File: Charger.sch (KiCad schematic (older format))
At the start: 65 parts, among them Q1 AO4407A, Q10 AON7400A, Q11 AON7400A, Q8 AON7400A, Q9 AON7400A, U1 bq2477x

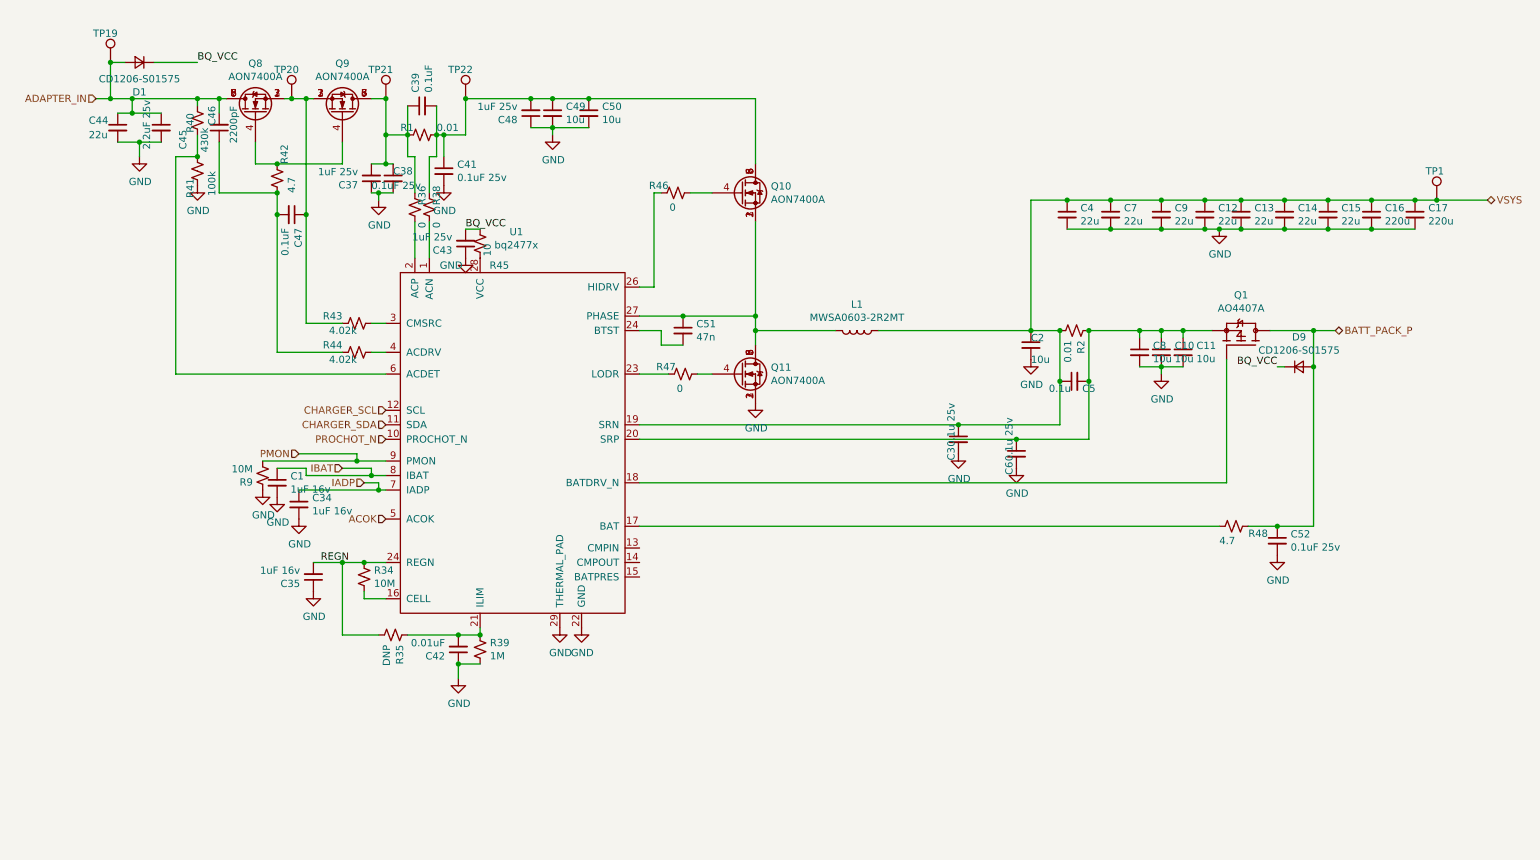
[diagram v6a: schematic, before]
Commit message: Replaced old charger to support JLC assembly. Very close now!
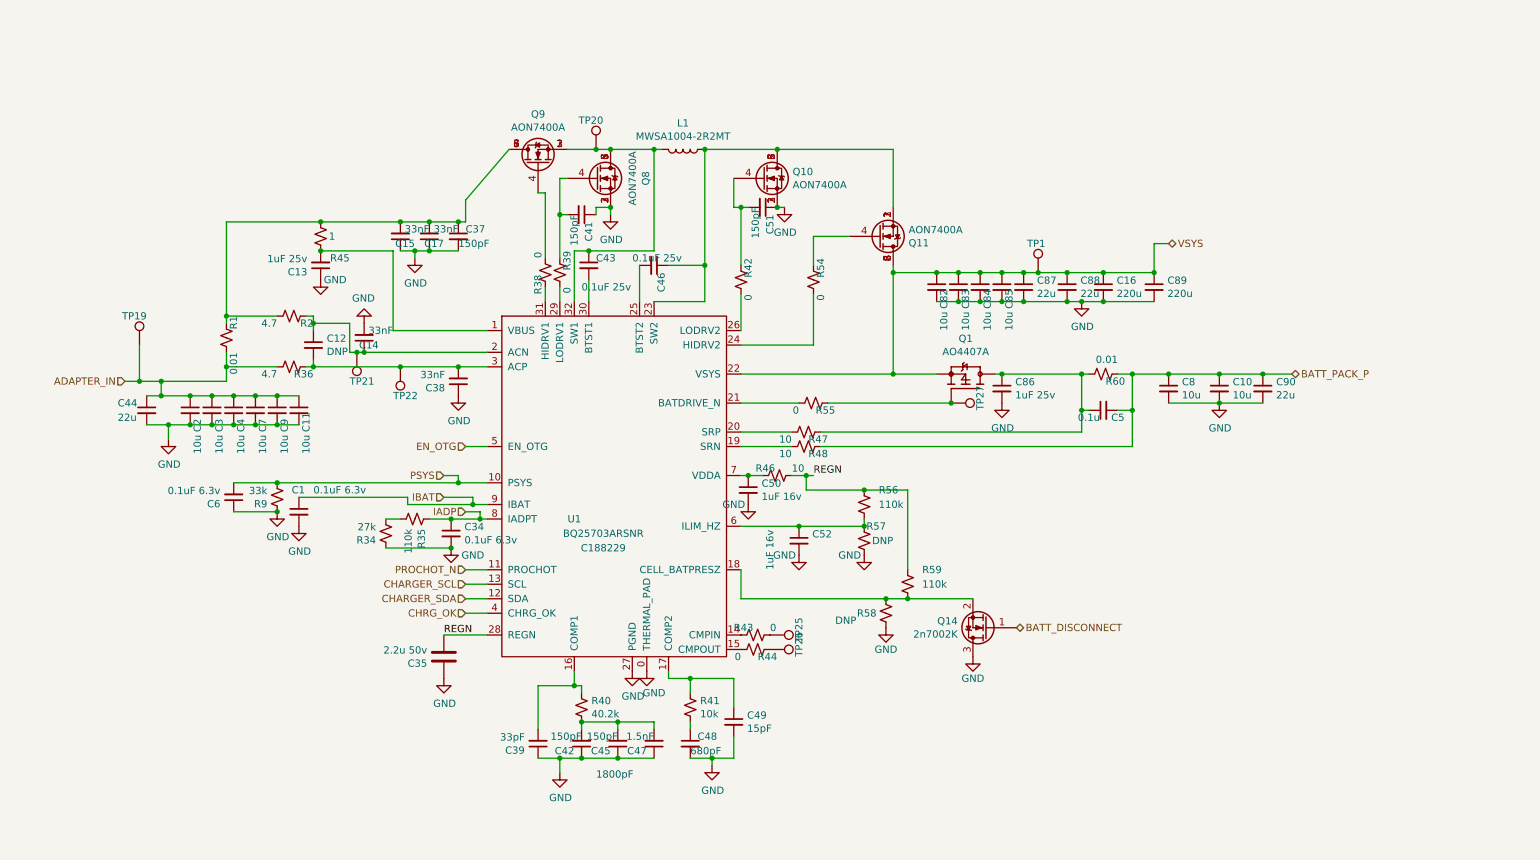
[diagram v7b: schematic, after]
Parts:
- removed C35: 1uF 16v, lc_lib:0402_C, symbol Device:C_Small
- removed D1, D9: CD1206-S01575, lc_lib:SOD-123, symbol Device:D_Small
- removed U1: bq2477x, SmartBattery:QFN40P400X400X80-29N, symbol SmartBattery:bq2477x
- added C35: 2.2u 50v, lc_lib:0805_C, symbol Device:C
- added C82, C83, C84, C85: 10u, lc_lib:0805_C, symbol Device:C_Small
- added C86: 1uF 25v, lc_lib:0402_C, symbol Device:C_Small
- added C87, C88, C90: 22u, lc_lib:0805_C, symbol Device:C_Small
- added C89: 220u, Capacitor_SMD:C_Elec_8x10.2, symbol Device:C_Small
- added Q14: 2n7002K, Package_TO_SOT_SMD:SOT-23, symbol Device:Q_NMOS_GSD
- added R54, R55: 0, lc_lib:0402_R, symbol Device:R_Small_US
- added R56, R59: 110k, lc_lib:0402_R, symbol Device:R_Small_US
- added R57, R58: DNP, lc_lib:0402_R, symbol Device:R_Small_US
- added R60: 0.01, lc_lib:2512_R, symbol Device:R_Small_US
- added TP25, TP26, TP27: TestPoint, TestPoint:TestPoint_Pad_D2.0mm, symbol Connector:TestPoint
- added U1: BQ25703ARSNR, lc_lib:VQFN-32_4X4X04P, symbol SmartBattery:BQ25703ARSNR
- C1: value 1uF 16v -> 0.1uF 6.3v; LCSC C52923 -> C1525
- C11: LCSC (none) -> C15850; SKU CC0805KKX5R8BB106 -> (none)
- C12: value 22u -> DNP; footprint lc_lib:0805_C -> lc_lib:0402_C; SKU CL21A226MAQNNNE -> (none)
- C13: value 22u -> 1uF 25v; footprint lc_lib:0805_C -> lc_lib:0402_C; SKU CL21A226MAQNNNE -> (none); lcsc (none) -> C52923
- C14, C15: value 22u -> 33nF; footprint lc_lib:0805_C -> lc_lib:0402_C; LCSC (none) -> C1585; SKU CL21A226MAQNNNE -> (none)
- C16: LCSC (none) -> C311611; SKU RVT1V221M0810 -> (none)
- C17: value 220u -> 33nF; footprint Capacitor_SMD:C_Elec_8x10.2 -> lc_lib:0402_C; LCSC (none) -> C1585; SKU RVT1V221M0810 -> (none)
- C3: value 0.1u 25v -> 10u; footprint lc_lib:0402_C -> lc_lib:0805_C; LCSC (none) -> C15850
- C34: value 1uF 16v -> 0.1uF 6.3v; lcsc (none) -> C1525
- C37: value 1uF 25v -> 150pF; lcsc (none) -> C1527
- C38: value 0.1uF 25v -> 33nF; LCSC (none) -> C1585
- C39: value 0.1uF -> 33pF; LCSC (none) -> C1562
- C4, C7, C9: value 22u -> 10u; LCSC (none) -> C15850; SKU CL21A226MAQNNNE -> (none)
- C41: value 0.1uF 25v -> 150pF; lcsc (none) -> C1527
- C42: value 0.01uF -> 150pF; lcsc (none) -> C1527
- C43: value 1uF 25v -> 0.1uF 25v; lcsc (none) -> C1525
- C44: LCSC (none) -> C45783; SKU CL21A226MAQNNNE -> (none)
- C45: value 2.2uF 25v -> 150pF; footprint lc_lib:0805_C -> lc_lib:0402_C; lcsc (none) -> C1527
- C46: value 2200pF -> 0.1uF 25v; lcsc (none) -> C1525
- C47: value 0.1uF -> 1.5nF; lcsc (none) -> C23967
- C48: value 1uF 25v -> 680pF; footprint lc_lib:0402_C -> lc_lib:0603_C; SKU CC0805KKX5R8BB106 -> (none); lcsc (none) -> C1630
- C49: value 10u -> 15pF; footprint lc_lib:0805_C -> lc_lib:0402_C; LCSC (none) -> C1548; SKU CC0805KKX5R8BB106 -> (none)
- C50: value 10u -> 1uF 16v; footprint lc_lib:0805_C -> lc_lib:0402_C; SKU CC0805KKX5R8BB106 -> (none); lcsc (none) -> C52923
- C51: value 47n -> 150pF; lcsc (none) -> C1527
- C52: value 0.1uF 25v -> 1uF 16v; lcsc (none) -> C52923
- C6: value 0.1u 25v -> 0.1uF 6.3v; lcsc (none) -> C1525
- L1: value MWSA0603-2R2MT -> MWSA1004-2R2MT; footprint SmartBattery:MWSA0603 -> SmartBattery:L_10.3x11.5_H4; LCSC (none) -> C149550; SKU MWSA0603-2R2MT -> (none)
- Q1: LCSC (none) -> C16072
- Q10, Q11, Q8, Q9: LCSC (none) -> C85734; SKU AON7400A -> (none)
- R1: lcsc (none) -> C127692
- R2: value 0.01 -> 4.7; footprint lc_lib:2512_R -> lc_lib:0402_R; lcsc (none) -> C23164
- R34: value 10M -> 27k; footprint lc_lib:0402_R -> lc_lib:0603_R; lcsc (none) -> C25771
- R35: value DNP -> 110k; footprint lc_lib:0402_R -> lc_lib:0603_R; lcsc (none) -> C25805
- R36: value 0 -> 4.7; lcsc (none) -> C23164
- R39: value 1M -> 0
- R40: value 430k -> 40.2k; footprint lc_lib:0402_R -> lc_lib:0603_R; lcsc (none) -> C12447
- R41: value 100k -> 10k; lcsc (none) -> C25744
- R42: value 4.7 -> 0
- R43, R44: value 4.02k -> 0
- R45: value 10 -> 1; lcsc (none) -> C25086
- R46, R47: value 0 -> 10; lcsc (none) -> C25123
- R48: value 4.7 -> 10; lcsc (none) -> C25123
- R9: value 10M -> 33k; lcsc (none) -> C25779
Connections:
- net ADAPTER_IN: now also C11.1, C2.1, C3.1, C4.1, C7.1, C9.1, R1.1, R36.1; no longer C45.1, C46.2, Q8.5 (D), Q8.6 (D), Q8.7 (D), Q8.8 (D), R40.2
- net BATT_PACK_P: now also C10.1, C5.2, C8.1, R48.2, C90.1, R60.2; no longer C52.1, Q1.5, Q1.6, Q1.7, Q1.8, R48.1
- net CHARGER_SCL: now also U1.13 (SCL)
- net CHARGER_SDA: now also U1.12 (SDA)
- net GND: now also C13.1, C15.1, C17.1, C37.2, C38.1, C39.1, C41.1, C45.1, C47.1, C48.2, C51.1, C6.1, Q10.1 (S), Q10.2 (S), Q10.3 (S), Q8.1 (S), Q8.2 (S), Q8.3 (S), R34.1, C35.1, C82.2, C83.2, C84.2, C85.2, C86.2, C87.2, C88.2, C89.2, C90.2, Q14.3 (D), R57.1, R58.2, U1.0 (THERMAL_PAD), U1.27 (PGND); no longer C12.2, C13.2, C15.2, C17.2, C37.1, C38.2, C41.2, C43.1, C45.2, C48.1, C6.2, Q11.1 (S), Q11.2 (S), Q11.3 (S), R39.2, R41.1
- net IADP: now also R35.1, U1.8 (IADPT)
- net IBAT: now also U1.9 (IBAT)
- net PROCHOT_N: now also U1.11 (PROCHOT)
- net REGN: now also R46.1, C35.2, R56.1, R59.1, U1.28 (REGN); no longer R34.1, R35.2
- net VSYS: now also Q1.1, Q1.2, Q1.3, Q11.5 (D), Q11.6 (D), Q11.7 (D), Q11.8 (D), C82.1, C83.1, C84.1, C85.1, C87.1, C88.1, C89.1, U1.22 (VSYS); no longer C12.1, C13.1, C14.1, C15.1, C17.1, C2.1, C3.1, C4.1, C5.1, C7.1, C9.1, L1.1, R2.2
- net at R38.1: now also Q9.4 (G)
- net at R34.2: now also R35.2
- net at Q1.4: now also R55.2, TP27.1
- net at R47.1: now also U1.20 (SRP)
- net at C51.2: now also Q10.4 (G), R42.2
- net at R45.1: now also C13.2, U1.1 (VBUS)
- net at R43.2: now also U1.14 (CMPIN)
- net at R44.2: now also TP26.1
- net at R40.1: now also C39.2, U1.16 (COMP1); no longer R41.2
- net at Q9.5 (D), Q9.6 (D), Q9.7 (D)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: now also C15.2, C17.2, C37.1, R2.1, R45.2; no longer C37.2, C38.1, C39.1, R36.2, TP21.1
- net at R46.2: now also C50.1, U1.7 (VDDA); no longer Q10.4 (G)
- net at R47.2: now also C5.1, Q1.5, Q1.6, Q1.7, Q1.8, C86.1, R60.1; no longer Q11.4 (G)
- net BQ_VCC: no longer names the net of C43.2
- net BQ_VCC: now also U1.30 (BTST1); no longer R45.2
- net PMON renamed PSYS
- net PSYS: now also C6.2, U1.10 (PSYS)
- new net: C46.1, L1.1, Q10.5 (D), Q10.6 (D), Q10.7 (D), Q10.8 (D), Q11.1 (S), Q11.2 (S), Q11.3 (S), U1.23 (SW2)
- new net: C43.1, L1.2, Q8.5 (D), Q8.6 (D), Q8.7 (D), Q8.8 (D), Q9.1 (S), Q9.2 (S), Q9.3 (S), TP20.1, U1.32 (SW1)
- new net: C12.2, C38.2, R36.2, TP22.1, U1.3 (ACP)
- new net: C12.1, C14.1, R2.2, TP21.1, U1.2 (ACN)
- new net: R44.1, U1.15 (CMPOUT)
- new net: C49.1, R41.1, U1.17 (COMP2)
- new net: Q14.2 (S), R58.1, R59.2, U1.18 (CELL_BATPRESZ)
- new net: R48.1, U1.19 (SRN)
- new net: R55.1, U1.21 (BATDRIVE_N)
- new net: R54.1, U1.24 (HIDRV2)
- new net: C46.2, U1.25 (BTST2)
- new net: R42.1, U1.26 (LODRV2)
- new net: R39.1, U1.29 (LODRV1)
- new net: R38.2, U1.31 (HIDRV1)
- new net: C52.1, R56.2, R57.2, U1.6 (ILIM_HZ)
- new net: C42.2, C45.2, C47.2, R40.2
- new net: C48.1, R41.2
- new net: C41.2, Q8.4 (G), R39.2
- new net: Q11.4 (G), R54.2
- new net: R43.1, TP25.1
- new net BATT_DISCONNECT: Q14.1 (G)
- new net CHRG_OK: U1.4 (CHRG_OK)
- new net EN_OTG: U1.5 (EN_OTG)
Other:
- note added: "1800pF\n"
- moved on the sheet: C1, C10, C16, C34, C44, C5, C8, L1, Q1, Q10, Q11, Q8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

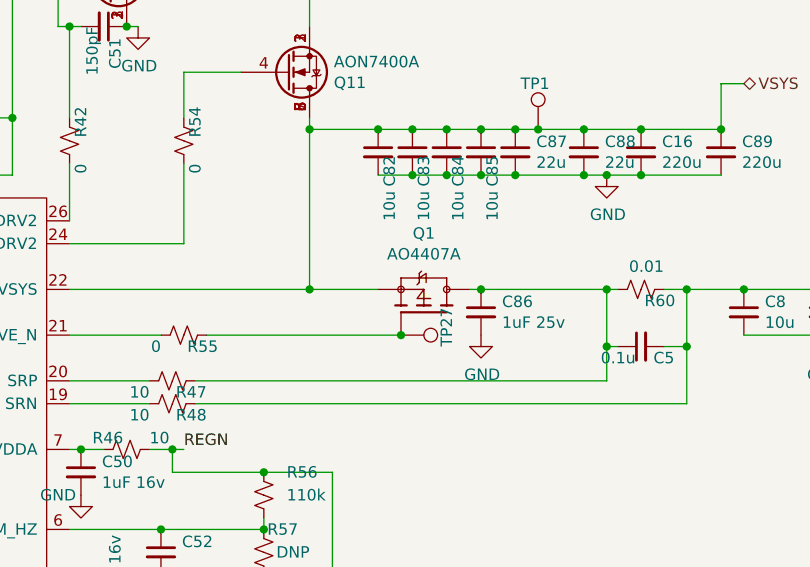
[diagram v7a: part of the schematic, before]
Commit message: Both type-c ports are done! Only outputstage left.
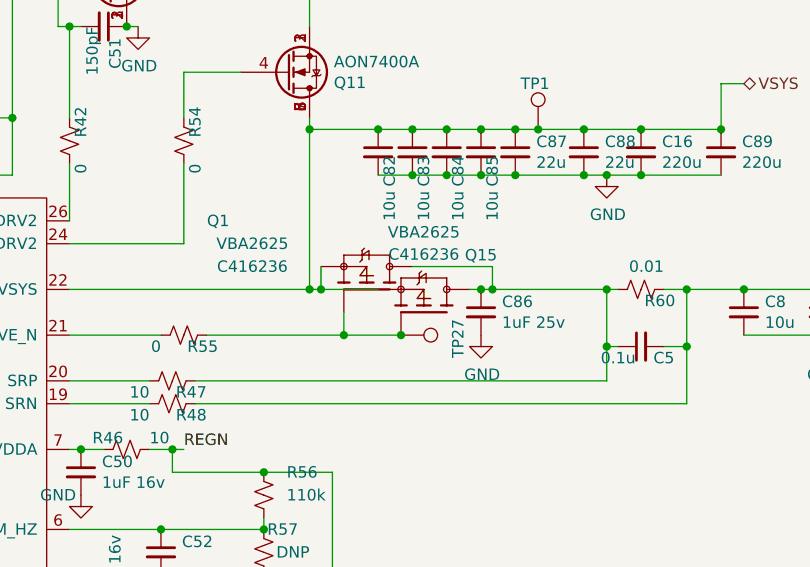
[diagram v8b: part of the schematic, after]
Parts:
- removed Q1: AO4407A, SmartBattery:SOIC127P600X175-8N, symbol SmartBattery:AO4407A
- added Q1, Q15: VBA2625, SmartBattery:SOIC127P600X175-8N, symbol SmartBattery:VBA2625
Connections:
- net VSYS: now also Q1.1, Q1.2, Q1.3, Q15.1, Q15.2, Q15.3
- net at R55.2, TP27.1: now also Q1.4, Q15.4
- net at C5.1, C86.1, R47.2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: now also Q1.5, Q1.6, Q1.7, Q1.8, Q15.5, Q15.6, Q15.7, Q15.8
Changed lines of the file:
@@
 $Descr A4 11693 8268
 encoding utf-8
-Sheet 2 6
+Sheet 2 8
 Title ""
 Date ""
@@
 Text HLabel 9250 3400 2    50   BiDi ~ 0
 BATT_PACK_P
-$Comp
-L SmartBattery:AO4407A Q1
-U 1 1 5FDAE275
-P 7000 3500
-F 0 "Q1" V 7345 3500 50  0000 C CNN
-F 1 "AO4407A" V 7254 3500 50  0000 C CNN
-F 2 "SmartBattery:SOIC127P600X175-8N" H 7000 3500 50  0001 L BNN
-F 3 "" H 7000 3500 50  0001 L BNN
-F 4 "Alpha & Omega Semiconductor" H 7000 3500 50  0001 L BNN "MANUFACTURER"
-F 5 "I" H 7000 3500 50  0001 L BNN "PARTREV"
-F 6 "IPC 7351B" H 7000 3500 50  0001 L BNN "STANDARD"
-F 7 "1.75 mm" H 7000 3500 50  0001 L BNN "MAXIMUM_PACKAGE_HEIGHT"
-F 8 "C16072" V 7000 3500 50  0001 C CNN "LCSC"
-	1    7000 3500
-	0    -1   -1   0
-$EndComp
 $Comp
 L Device:C_Small C10
@@
 Connection ~ 8300 2700
 Wire Wire Line
-	6800 3400 6500 3400
+	6800 3400 6550 3400
 Connection ~ 6500 3400
 Wire Wire Line
@@
 $EndComp
 Wire Wire Line
-	6050 3600 6900 3600
+	6050 3600 6650 3600
 $Comp
 L Connector:TestPoint TP?
@@
 AR Path="/5FD15753/60964FD3" Ref="TP?"  Part="1"
 AR Path="/5FD99B08/60964FD3" Ref="TP27"  Part="1"
-F 0 "TP27" H 6950 3800 50  0000 R CNN
+F 0 "TP27" H 7000 3850 50  0000 R CNN
 F 1 "TestPoint" H 6350 3650 50  0001 R CNN
 F 2 "TestPoint:TestPoint_Pad_D2.0mm" H 7100 3600 50  0001 C CNN
@@
 	0    1    1    0
 $EndComp
-Connection ~ 6900 3600
 $Comp
 L Device:C_Small C86
@@
 Connection ~ 7800 3400
 Wire Wire Line
-	7800 3400 7250 3400
+	7800 3400 7300 3400
 Wire Wire Line
 	8050 3650 8150 3650
@@
 	0    1    1    0
 $EndComp
+$Comp
+L SmartBattery:VBA2625 Q15
+U 1 1 5FF325EA
+P 7000 3500
+F 0 "Q15" V 7250 3250 50  0000 C CNN
+F 1 "VBA2625" V 7350 3500 50  0000 C CNN
+F 2 "SmartBattery:SOIC127P600X175-8N" H 7000 3500 50  0001 L BNN
+F 3 "" H 7000 3500 50  0001 L BNN
+F 4 "Alpha & Omega Semiconductor" H 7000 3500 50  0001 L BNN "MANUFACTURER"
+F 5 "I" H 7000 3500 50  0001 L BNN "PARTREV"
+F 6 "IPC 7351B" H 7000 3500 50  0001 L BNN "STANDARD"
+F 7 "1.75 mm" H 7000 3500 50  0001 L BNN "MAXIMUM_PACKAGE_HEIGHT"
+F 8 "C416236" V 7253 3500 50  0000 C CNN "lcsc"
+	1    7000 3500
+	0    -1   -1   0
+$EndComp
+Connection ~ 6900 3600
+$Comp
+L SmartBattery:VBA2625 Q1
+U 1 1 5FF6C0C9
+P 6750 3400
+F 0 "Q1" V 7050 4050 50  0000 C CNN
+F 1 "VBA2625" V 6950 3900 50  0000 C CNN
+F 2 "SmartBattery:SOIC127P600X175-8N" H 6750 3400 50  0001 L BNN
+F 3 "" H 6750 3400 50  0001 L BNN
+F 4 "Alpha & Omega Semiconductor" H 6750 3400 50  0001 L BNN "MANUFACTURER"
+F 5 "I" H 6750 3400 50  0001 L BNN "PARTREV"
+F 6 "IPC 7351B" H 6750 3400 50  0001 L BNN "STANDARD"
+F 7 "1.75 mm" H 6750 3400 50  0001 L BNN "MAXIMUM_PACKAGE_HEIGHT"
+F 8 "C416236" V 6850 3900 50  0000 C CNN "lcsc"
+	1    6750 3400
+	0    -1   -1   0
+$EndComp
+Wire Wire Line
+	6650 3500 6650 3600
+Connection ~ 6650 3600
+Wire Wire Line
+	6650 3600 6900 3600
+Wire Wire Line
+	6550 3300 6550 3400
+Connection ~ 6550 3400
+Wire Wire Line
+	6550 3400 6500 3400
+Wire Wire Line
+	6950 3300 7300 3300
+Wire Wire Line
+	7300 3300 7300 3400
+Connection ~ 7300 3400
+Wire Wire Line
+	7300 3400 7250 3400
 $EndSCHEMATC
